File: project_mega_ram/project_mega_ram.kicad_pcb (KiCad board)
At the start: 2 copper layers, 100.7 x 87.3 mm, 28 parts, among them U1 74LS670, U10 74LS02, U11 74LS139, U12 CS18LV10245, U2 CS18LV10245, U3 74LS670, U4 74LS157, U5 74LS157, U6 74LS08, U7 74LS32, U8 74LS74, U9 74LS32

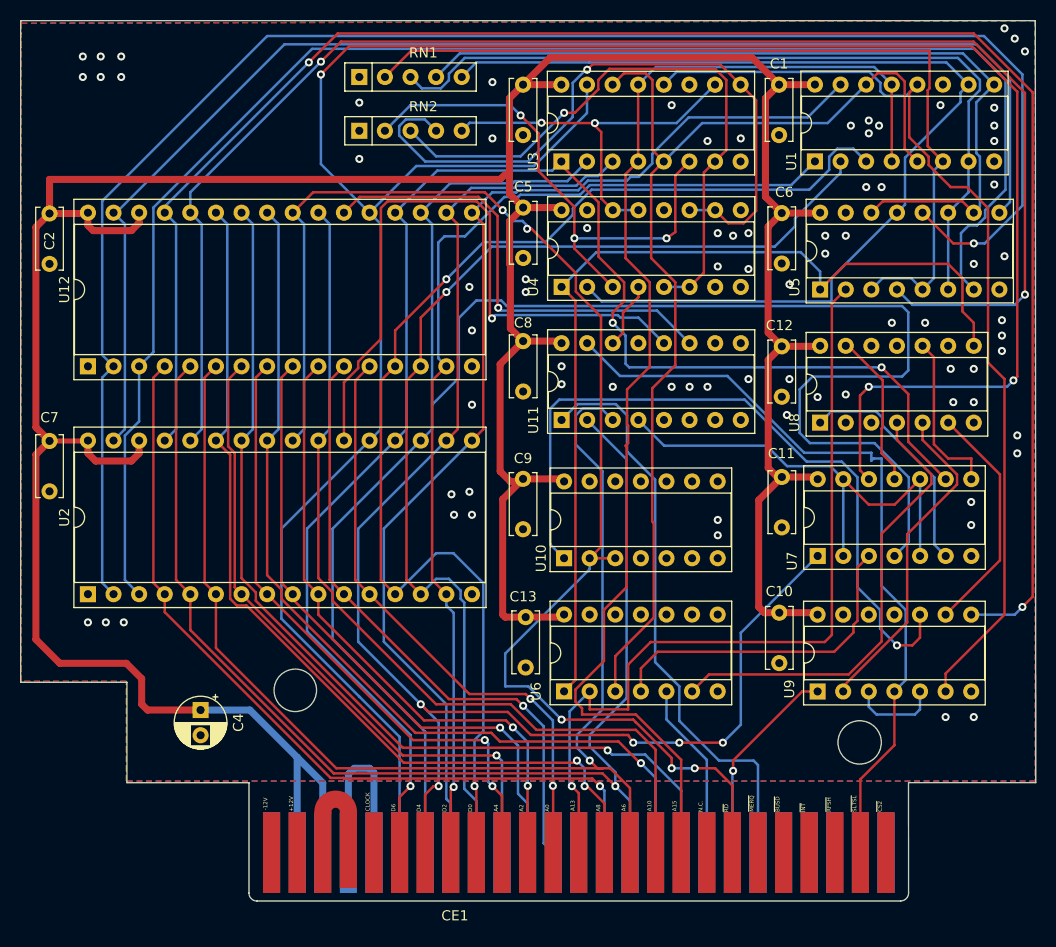
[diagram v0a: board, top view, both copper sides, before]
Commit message: modified project_mega_ram design
Signed-off-by: Youngki Park <ykp7409@gmail.com>
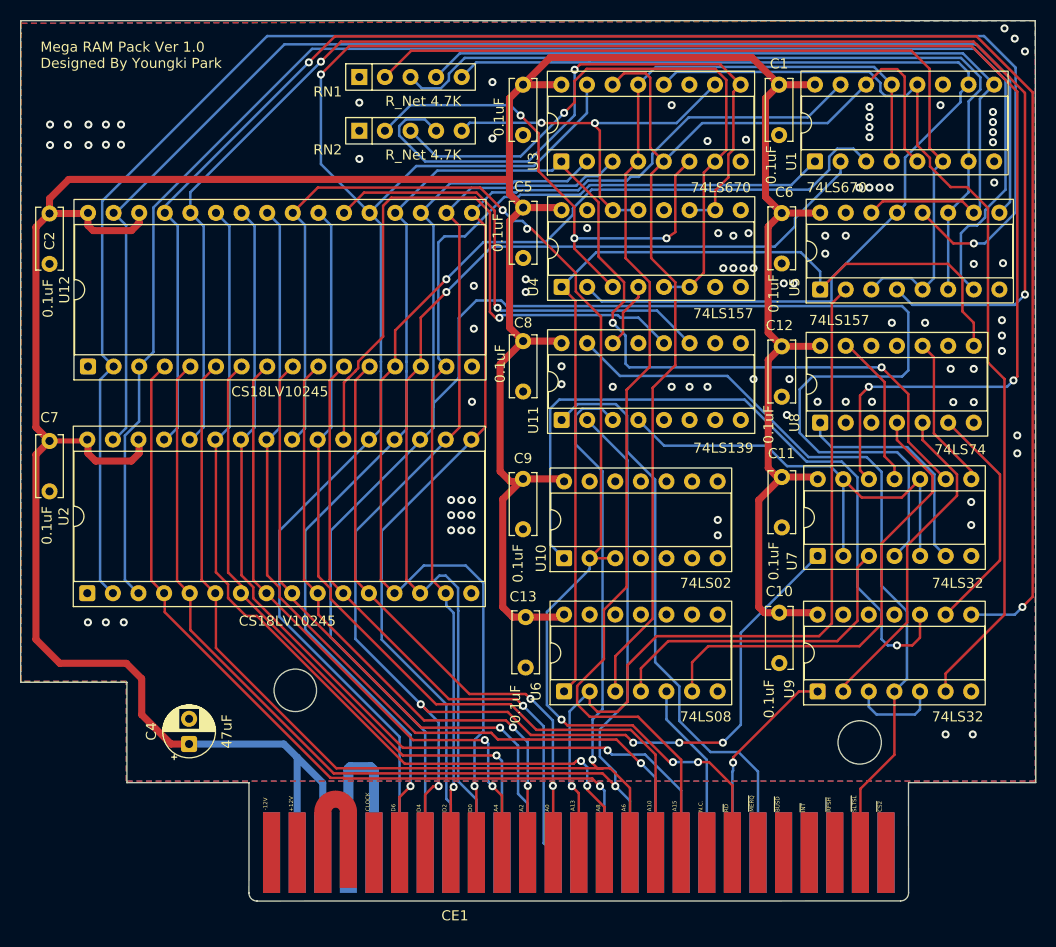
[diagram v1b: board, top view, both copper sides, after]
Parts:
- moved C4 3.56 mm to (103.0, 115.7), turned to 90 degrees
- moved U2 0.12 mm to (92.9, 100.7)
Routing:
- net //RD: track 138.3 -> 133.5 mm
- net Net-(RN2-R3): track 67.9 -> 63.8 mm
- net /D5: track 188.6 -> 190.0 mm
- net Net-(U8B-~{S}): track 16.6 -> 15.2 mm
- net //STLSL: track 76.5 -> 75.2 mm
- net /A13: track 83.5 -> 82.2 mm
- net Net-(RN1-R1): track 86.4 -> 85.2 mm
- net /A6: track 125.0 -> 124.0 mm
- net /D0: track 122.0 -> 121.0 mm
- net /A7: track 123.6 -> 122.8 mm
- net Net-(U8A-~{S}): track 46.0 -> 46.8 mm
- net +5V: track 354.7 -> 353.9 mm
- net Net-(RN1-R4): track 103.7 -> 104.4 mm
- net Net-(RN2-R2): track 61.6 -> 62.3 mm
- net //670WE: track 95.4 -> 94.8 mm
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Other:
- board text added: "Mega RAM Pack Ver 1.0 Designed By Youngki Park"

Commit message: Modify Project mega ram card
Signed-off-by: Youngki Park <ykp7409@gmail.com>
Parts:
- CE1: value Card_Edge_Connector_MSX -> card_edge_connector_msx
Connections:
- U12 pad 29: /RW -> //WR
- U2 pad 29: /RW -> //WR
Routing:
- net //WR: track 20.6 -> 227.6 mm, vias 1 -> 3
- net /RW: track 176.6 -> 0.00 mm, vias 2 -> 0
- net /D2: track 103.2 -> 112.7 mm
- net /D1: track 109.8 -> 118.1 mm
- net /D0: track 121.0 -> 126.7 mm
- net /A0: track 60.3 -> 65.3 mm
- net /A5: track 65.5 -> 70.2 mm
- net /MA13: track 150.6 -> 154.9 mm
- net /A8: track 91.9 -> 95.9 mm
- net /A1: track 61.9 -> 65.8 mm
- net /MA14: track 156.1 -> 159.9 mm
- net /A10: track 88.2 -> 91.5 mm
- net /MA15: track 134.7 -> 136.9 mm
- net /A2: track 62.8 -> 64.8 mm
- net /A3: track 63.6 -> 65.4 mm
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
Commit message: modified PCB : Signed-off-by: ykp74 <ykp7409@gmail.com>
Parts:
- C4: value 47uF -> 100uF
- moved C12 0.50 mm to (162.3, 76.2)
- moved C1 0.26 mm to (161.8, 50.3)
- moved C11 0.23 mm to (161.8, 89.4)
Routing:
- net Net-(RN2-R3): track 63.8 -> 52.1 mm
- net /D6: track 154.5 -> 159.0 mm
- net +5V: track 353.9 -> 358.2 mm
- net /MA14: track 159.9 -> 156.3 mm
- net //WR: track 227.6 -> 224.8 mm
- net Net-(RN2-R1): track 53.4 -> 55.5 mm
- net /MA13: track 154.9 -> 153.3 mm
- net Net-(RN2-R4): track 39.1 -> 40.5 mm
- net Net-(RN2-R2): track 62.3 -> 63.6 mm
- net /MA15: track 136.9 -> 135.8 mm
- net /D7: track 242.7 -> 243.7 mm
- net Net-(RN1-R2): track 81.8 -> 82.8 mm
- net //670WE: track 94.8 -> 95.7 mm
- net Net-(RN1-R3): track 82.3 -> 83.1 mm
- net /RAM_0: track 65.1 -> 65.9 mm
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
